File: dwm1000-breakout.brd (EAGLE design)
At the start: 26.2 x 21.6 mm, 9 parts, among them U2 DWM1000

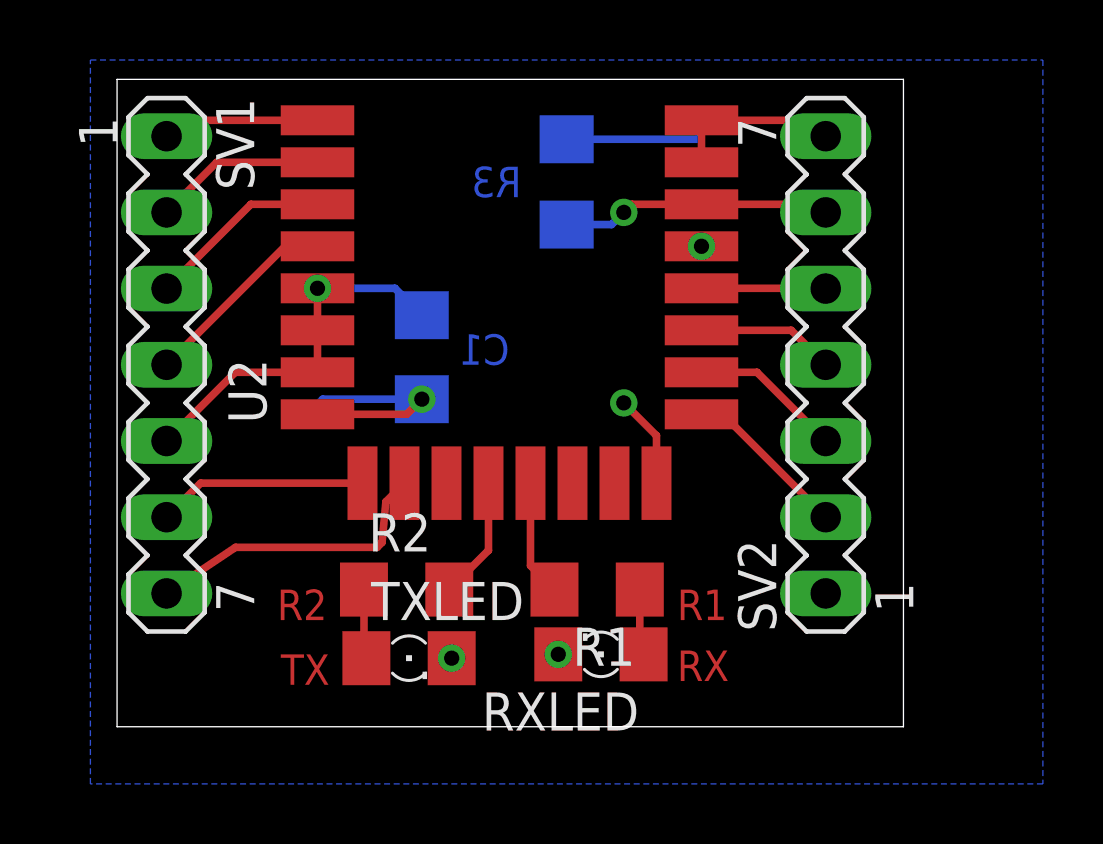
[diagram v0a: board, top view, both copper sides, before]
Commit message: renamed and laid out a little better i hope
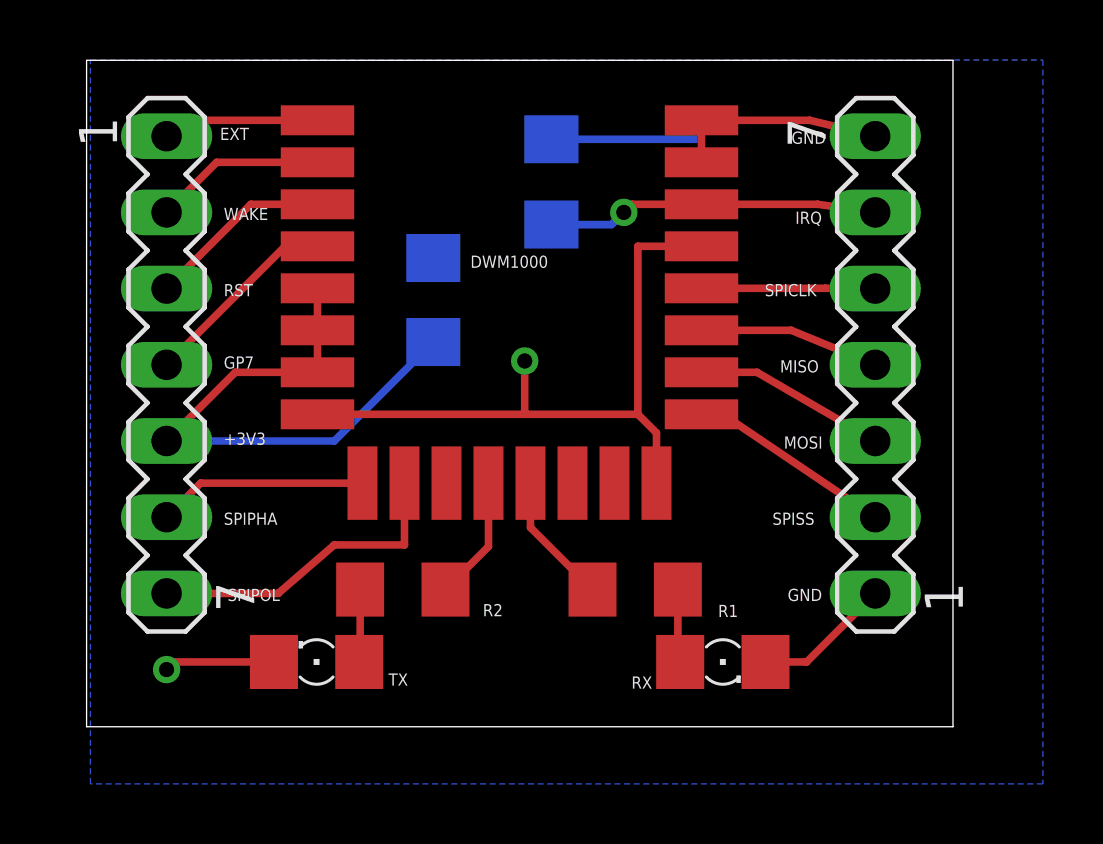
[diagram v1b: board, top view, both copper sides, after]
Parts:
- removed RXLED, TXLED: (no value), led:1206
- added RX, TX: (no value), led:1206
- moved C1 1.94 mm to (10.2, 17.4), turned to 90 degrees
- moved SV2 1.65 mm to (24.9, 15.2)
- moved R1 1.27 mm to (16.9, 7.75)
- moved R3 0.51 mm to (14.1, 21.3)
- moved R2 0.13 mm to (9.14, 7.75)
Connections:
- net GND: now also RX.C, TX.C; no longer RXLED.C, TXLED.C
- net N$1: now also RX.A; no longer RXLED.A
- net N$2: now also TX.A; no longer TXLED.A
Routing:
- net GND: track 20.5 -> 43.3 mm, vias 5 -> 2
- net +3V3: track 12.6 -> 19.0 mm, vias 1 -> 0
- net IRQ: track 9.03 -> 11.1 mm
- net SPICLK: track 4.15 -> 5.79 mm
- net MISO: track 4.62 -> 6.02 mm
- net MOSI: track 5.09 -> 6.41 mm
- net SPISS: track 5.56 -> 6.84 mm
- net SPIPOL: track 9.95 -> 10.6 mm
- net RXLED: track 3.88 -> 4.41 mm
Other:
- board size 26.2 x 21.6 mm -> 28.9 x 22.2 mm
- board text added: "+3V3"
- board text added: "EXT"
- board text added: "GND"
- board text added: "GP7"
- board text added: "IRQ"
- board text added: "MISO"
- board text added: "MOSI"
- board text added: "RST"
- board text added: "SPICLK"
- board text added: "SPIPHA"
- board text added: "SPIPOL"
- board text added: "SPISS"
- board text added: "WAKE"
- board text removed: "C1"
- board text removed: "R1"
- board text removed: "R2"
- board text removed: "R3"
- board text removed: "RX"
- board text removed: "TX"

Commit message: used oshpark's DRU file
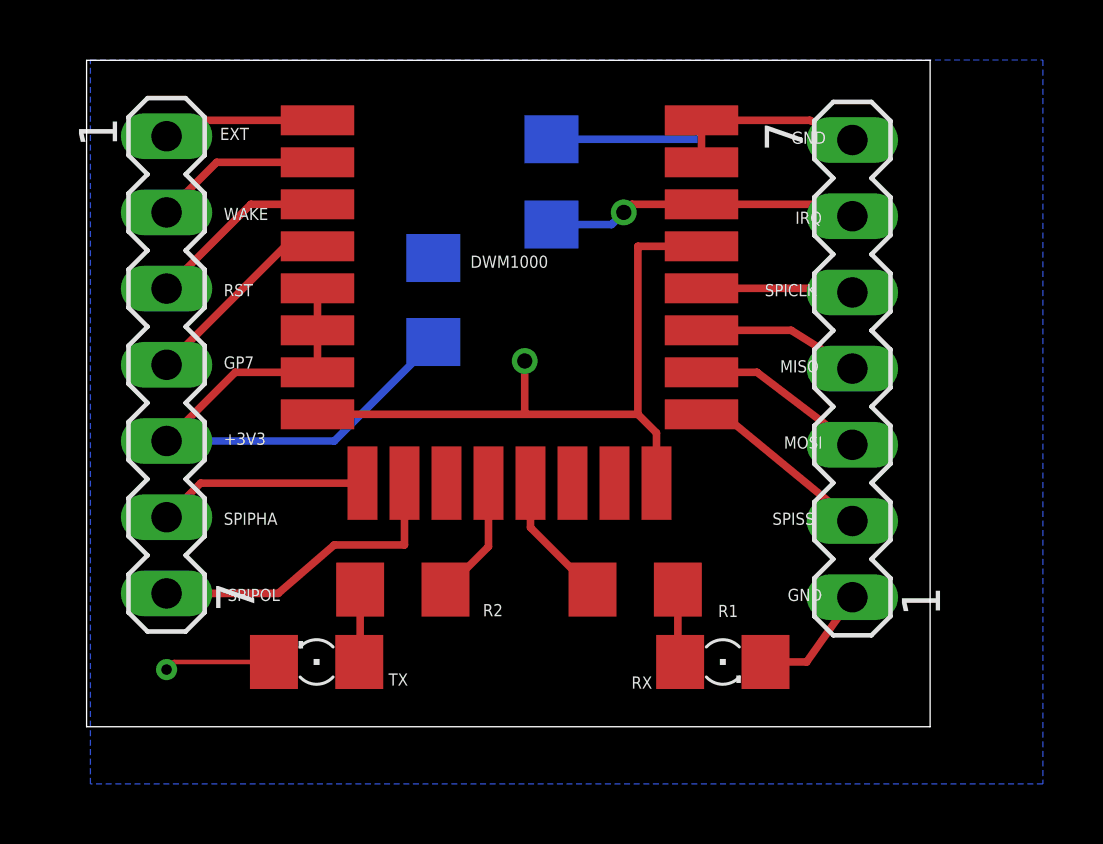
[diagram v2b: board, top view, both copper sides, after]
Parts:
- C1: value (none) -> 0.1uF
- R1, R2: value (none) -> 470
- R3: value (none) -> 100k
- moved SV2 0.77 mm to (24.1, 15.1)
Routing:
- net GND: track 43.3 -> 42.0 mm
- net SPICLK: track 5.79 -> 5.04 mm
- net IRQ: track 11.1 -> 10.4 mm
- net MISO: track 6.02 -> 5.40 mm
- net MOSI: track 6.41 -> 5.84 mm
- net SPISS: track 6.84 -> 6.31 mm
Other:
- board size 28.9 x 22.2 mm -> 28.1 x 22.2 mm

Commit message: added a power indicator LED
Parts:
- added PWR: (no value), led:1206
- added R4: (no value), rcl:R1206
- moved TX 13.7 mm to (19.8, 7.11), turned to 90 degrees
- moved R2 3.24 mm to (12.3, 7.11), turned to 90 degrees
- moved RX 2.80 mm to (17.7, 7.11), turned to 90 degrees
- moved R1 2.01 mm to (15.0, 7.11), turned to 90 degrees
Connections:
- new net N$3: PWR.A, R4.2
- net +3V3: now also R4.1
- net GND: now also PWR.C
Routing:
- net N$3: track 0.00 -> 7.75 mm, vias 0 -> 1
- net N$2: track 2.43 -> 8.39 mm
- net +3V3: track 19.0 -> 24.5 mm, vias 0 -> 1
- net GND: track 42.0 -> 47.0 mm
- net TXLED: track 4.14 -> 2.89 mm
- net RXLED: track 4.41 -> 3.42 mm
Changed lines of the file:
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@@
 <layer number="25" name="tNames" color="7" fill="1" visible="yes" active="yes"/>
 <layer number="26" name="bNames" color="7" fill="1" visible="yes" active="yes"/>
-<layer number="27" name="tValues" color="7" fill="1" visible="yes" active="yes"/>
-<layer number="28" name="bValues" color="7" fill="1" visible="yes" active="yes"/>
+<layer number="27" name="tValues" color="7" fill="1" visible="no" active="yes"/>
+<layer number="28" name="bValues" color="7" fill="1" visible="no" active="yes"/>
 <layer number="29" name="tStop" color="7" fill="3" visible="no" active="yes"/>
 <layer number="30" name="bStop" color="7" fill="6" visible="no" active="yes"/>
@@
 <attribute name="VALUE" x="7.62" y="16.129" size="1.27" layer="28" rot="MR90"/>
 </element>
-<element name="RX" library="led" library_urn="urn:adsk.eagle:library:259" package="1206" value="" x="19.812" y="5.334" smashed="yes">
-<attribute name="NAME" x="16.764" y="4.445" size="0.4064" layer="25" font="vector"/>
-<attribute name="VALUE" x="18.542" y="2.794" size="1.27" layer="27"/>
-</element>
-<element name="TX" library="led" library_urn="urn:adsk.eagle:library:259" package="1206" value="" x="6.27" y="5.334" smashed="yes" rot="R180">
-<attribute name="NAME" x="9.318" y="4.953" size="0.4064" layer="25" rot="R180"/>
-<attribute name="VALUE" x="7.54" y="7.874" size="1.27" layer="27" rot="R180"/>
-</element>
-<element name="R1" library="rcl" library_urn="urn:adsk.eagle:library:334" package="R1206" value="470" x="16.891" y="7.747" smashed="yes" rot="R180">
-<attribute name="NAME" x="20.32" y="7.239" size="0.4064" layer="25" rot="R180"/>
-<attribute name="VALUE" x="18.161" y="10.287" size="1.27" layer="27" rot="R180"/>
-</element>
-<element name="R2" library="rcl" library_urn="urn:adsk.eagle:library:334" package="R1206" value="470" x="9.144" y="7.747" smashed="yes">
-<attribute name="NAME" x="11.811" y="6.858" size="0.4064" layer="25"/>
-<attribute name="VALUE" x="7.874" y="5.207" size="1.27" layer="27"/>
+<element name="RX" library="led" library_urn="urn:adsk.eagle:library:259" package="1206" value="" x="17.653" y="7.112" smashed="yes" rot="R90">
+<attribute name="NAME" x="18.415" y="4.699" size="0.4064" layer="25" font="vector" rot="R180"/>
+<attribute name="VALUE" x="20.193" y="5.842" size="1.27" layer="27" rot="R90"/>
+</element>
+<element name="TX" library="led" library_urn="urn:adsk.eagle:library:259" package="1206" value="" x="19.812" y="7.112" smashed="yes" rot="R90">
+<attribute name="NAME" x="20.574" y="4.699" size="0.4064" layer="25" rot="R180"/>
+<attribute name="VALUE" x="22.352" y="5.842" size="1.27" layer="27" rot="R90"/>
+</element>
+<element name="R1" library="rcl" library_urn="urn:adsk.eagle:library:334" package="R1206" value="470" x="14.986" y="7.112" smashed="yes" rot="R90">
+<attribute name="NAME" x="14.859" y="4.445" size="0.4064" layer="25" rot="R180"/>
+<attribute name="VALUE" x="17.526" y="5.842" size="1.27" layer="27" rot="R90"/>
+</element>
+<element name="R2" library="rcl" library_urn="urn:adsk.eagle:library:334" package="R1206" value="470" x="12.319" y="7.112" smashed="yes" rot="R90">
+<attribute name="NAME" x="11.43" y="4.064" size="0.4064" layer="25"/>
+<attribute name="VALUE" x="14.859" y="5.842" size="1.27" layer="27" rot="R90"/>
 </element>
 <element name="R3" library="rcl" library_urn="urn:adsk.eagle:library:334" package="R1206" value="100k" x="14.097" y="21.336" smashed="yes" rot="MR270">
@@
 <attribute name="PRICE" value="20.95 USD" x="12.7" y="21.59" size="1.778" layer="27" display="off"/>
 <attribute name="VALUE" x="13.988" y="18.879" size="0.4064" layer="25" rot="R180"/>
+</element>
+<element name="PWR" library="led" library_urn="urn:adsk.eagle:library:259" package="1206" value="" x="5.588" y="4.826" smashed="yes" rot="R180">
+<attribute name="NAME" x="7.874" y="3.81" size="0.4064" layer="25" font="vector" rot="R180"/>
+<attribute name="VALUE" x="6.858" y="7.366" size="1.27" layer="27" rot="R180"/>
+</element>
+<element name="R4" library="rcl" library_urn="urn:adsk.eagle:library:334" package="R1206" value="" x="5.588" y="7.239" smashed="yes" rot="MR180">
+<attribute name="NAME" x="5.969" y="5.588" size="0.4064" layer="26" font="vector" rot="MR0"/>
+<attribute name="VALUE" x="4.318" y="9.779" size="1.27" layer="28" rot="MR180"/>
 </element>
 </elements>
@@
 <wire x1="22.711" y1="23.39" x2="24.13" y2="22.733" width="0.254" layer="1"/>
 <wire x1="19.1" y1="21.99" x2="19.1" y2="23.39" width="0.254" layer="1"/>
-<wire x1="21.234" y1="5.334" x2="22.606" y2="5.334" width="0.254" layer="1"/>
-<wire x1="22.606" y1="5.334" x2="24.13" y2="7.493" width="0.254" layer="1"/>
 <wire x1="17.6" y1="12.96986875" x2="17.6" y2="11.295" width="0.254" layer="1"/>
 <wire x1="6.3" y1="13.59" x2="13.208" y2="13.59" width="0.254" layer="1"/>
@@
 <wire x1="19.1" y1="19.19" x2="16.97986875" y2="19.19" width="0.254" layer="1"/>
 <wire x1="16.97986875" y1="19.19" x2="16.97986875" y2="13.59" width="0.254" layer="1"/>
-<wire x1="4.848" y1="5.334" x2="1.524" y2="5.334" width="0.1524" layer="1"/>
-<wire x1="1.524" y1="5.334" x2="1.27" y2="5.08" width="0.1524" layer="1"/>
+<contactref element="PWR" pad="C"/>
+<wire x1="4.166" y1="4.826" x2="1.524" y2="4.826" width="0.254" layer="1"/>
+<wire x1="1.524" y1="4.826" x2="1.27" y2="5.08" width="0.254" layer="1"/>
 <via x="1.27" y="5.08" extent="1-16" drill="0.35"/>
+<wire x1="17.653" y1="8.534" x2="19.812" y2="8.534" width="0.254" layer="1"/>
+<wire x1="19.812" y1="8.534" x2="23.089" y2="8.534" width="0.254" layer="1"/>
+<wire x1="23.089" y1="8.534" x2="24.13" y2="7.493" width="0.254" layer="1"/>
+<wire x1="17.6" y1="11.295" x2="17.6" y2="8.587" width="0.254" layer="1"/>
+<wire x1="17.6" y1="8.587" x2="17.653" y2="8.534" width="0.254" layer="1"/>
 </signal>
 <signal name="+3V3">
@@
 <wire x1="6.3" y1="16.39" x2="6.3" y2="14.99" width="0.254" layer="1"/>
 <wire x1="6.3" y1="16.39" x2="6.3" y2="17.79" width="0.254" layer="1"/>
-<wire x1="1.27" y1="12.7" x2="6.861" y2="12.7" width="0.254" layer="16"/>
+<wire x1="4.15514375" y1="12.7" x2="1.27" y2="12.7" width="0.254" layer="16"/>
+<wire x1="4.15514375" y1="12.7" x2="6.861" y2="12.7" width="0.254" layer="16"/>
 <wire x1="6.861" y1="12.7" x2="10.16" y2="15.999" width="0.254" layer="16"/>
+<contactref element="R4" pad="1"/>
+<wire x1="4.166" y1="7.239" x2="4.166" y2="12.68914375" width="0.254" layer="16"/>
+<wire x1="4.166" y1="12.68914375" x2="4.15514375" y2="12.7" width="0.254" layer="16"/>
+<via x="4.166" y="12.68914375" extent="1-16" drill="0.35"/>
 </signal>
 <signal name="MOSI">
@@
 <contactref element="U2" pad="12"/>
 <contactref element="R2" pad="2"/>
-<wire x1="12" y1="11.295" x2="12" y2="9.181" width="0.254" layer="1"/>
-<wire x1="12" y1="9.181" x2="10.566" y2="7.747" width="0.254" layer="1"/>
+<wire x1="12" y1="11.295" x2="12" y2="8.853" width="0.254" layer="1"/>
+<wire x1="12" y1="8.853" x2="12.319" y2="8.534" width="0.254" layer="1"/>
 </signal>
 <signal name="RXLED">
 <contactref element="U2" pad="13"/>
 <contactref element="R1" pad="2"/>
-<wire x1="13.4" y1="11.295" x2="13.4" y2="9.816" width="0.254" layer="1"/>
-<wire x1="13.4" y1="9.816" x2="15.469" y2="7.747" width="0.254" layer="1"/>
+<wire x1="13.4" y1="11.295" x2="13.4" y2="10.12" width="0.254" layer="1"/>
+<wire x1="13.4" y1="10.12" x2="14.986" y2="8.534" width="0.254" layer="1"/>
 </signal>
 <signal name="EXT">
@@
 <contactref element="R1" pad="1"/>
 <contactref element="RX" pad="A"/>
-<wire x1="18.313" y1="7.747" x2="18.313" y2="5.411" width="0.254" layer="1"/>
-<wire x1="18.313" y1="5.411" x2="18.39" y2="5.334" width="0.254" layer="1"/>
+<wire x1="14.986" y1="5.69" x2="17.653" y2="5.69" width="0.254" layer="1"/>
 </signal>
 <signal name="N$2">
 <contactref element="R2" pad="1"/>
 <contactref element="TX" pad="A"/>
-<wire x1="7.722" y1="7.747" x2="7.722" y2="5.364" width="0.254" layer="1"/>
-<wire x1="7.722" y1="5.364" x2="7.692" y2="5.334" width="0.254" layer="1"/>
+<wire x1="12.319" y1="5.69" x2="12.88936875" y2="5.69" width="0.254" layer="1"/>
+<wire x1="19.74963125" y1="5.69" x2="19.812" y2="5.69" width="0.254" layer="1"/>
+<wire x1="12.88936875" y1="5.69" x2="13.96876875" y2="4.6106" width="0.254" layer="1"/>
+<wire x1="18.67023125" y1="4.6106" x2="19.74963125" y2="5.69" width="0.254" layer="1"/>
+<wire x1="13.96876875" y1="4.6106" x2="18.67023125" y2="4.6106" width="0.254" layer="1"/>
+</signal>
+<signal name="N$3">
+<contactref element="R4" pad="2"/>
+<contactref element="PWR" pad="A"/>
+<wire x1="7.01" y1="4.826" x2="9.677" y2="4.826" width="0.254" layer="1"/>
+<via x="9.677" y="4.826" extent="1-16" drill="0.35"/>
+<wire x1="7.01" y1="7.239" x2="9.677" y2="7.239" width="0.254" layer="16"/>
+<wire x1="9.677" y1="7.239" x2="9.677" y2="4.826" width="0.254" layer="16"/>
 </signal>
 </signals>

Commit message: Rand's nitpicking
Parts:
- removed C1: 0.1uF, rcl:C1206
- added C2: (no value), Passives:C1210
- moved TX 7.15 mm to (12.7, 6.35), turned to 270 degrees
- moved PWR 3.18 mm to (8.38, 6.35), turned to 270 degrees
- moved R4 2.93 mm to (8.38, 6.35), turned to 90 degrees
- moved R3 2.56 mm to (15.2, 19.1)
- moved R1 2.17 mm to (17.0, 6.35), flipped to the bottom, turned to 270 degrees
- moved RX 0.99 mm to (17.0, 6.35), turned to 270 degrees
- moved R2 0.85 mm to (12.7, 6.35), flipped to the bottom, turned to 270 degrees
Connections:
- net +3V3: now also C2.P$1; no longer C1.1
- net GND: now also C2.P$2; no longer C1.2, RX.C, TX.C
- net N$1: now also R1.2, RX.C; no longer R1.1, RX.A
- net N$2: now also R2.2, TX.C; no longer R2.1, TX.A
- net RXLED: now also RX.A; no longer R1.2
- net TXLED: now also TX.A; no longer R2.2
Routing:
- net GND: track 47.0 -> 0.00 mm, vias 2 -> 5
- net IRQ: track 10.4 -> 15.9 mm
- net N$2: track 8.39 -> 4.19 mm, vias 0 -> 1
- net +3V3: track 24.5 -> 28.3 mm
- net N$1: track 2.67 -> 5.38 mm, vias 0 -> 1
- net N$3: track 7.75 -> 5.21 mm
- net RXLED: track 3.42 -> 5.93 mm
- net TXLED: track 2.89 -> 3.81 mm
- net GP7: track 6.67 -> 7.56 mm
- added copper zone on layer 1, net GND

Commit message: Whoops left some things unconnected. Fixed.
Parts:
- C2: value (none) -> 0.1uF
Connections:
- net GND: now also R1.1, R2.1
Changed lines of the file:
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@@
 <attribute name="VALUE" x="5.842" y="5.08" size="1.27" layer="28" rot="MR90"/>
 </element>
-<element name="C2" library="Passives" package="C1210" value="" x="10.16" y="19.05" rot="MR90">
+<element name="C2" library="Passives" package="C1210" value="0.1uF" x="10.16" y="19.05" rot="MR90">
 <attribute name="DIGIKEY" value="N/A" x="10.16" y="19.05" size="1.778" layer="28" rot="MR90" display="off"/>
 <attribute name="MPN" value="N/A" x="10.16" y="19.05" size="1.778" layer="28" rot="MR90" display="off"/>
@@
 <via x="15.24" y="22.86" extent="1-16" drill="0.635"/>
 <via x="12.7" y="15.24" extent="1-16" drill="0.635"/>
+<contactref element="R2" pad="1"/>
+<contactref element="R1" pad="1"/>
 </signal>
 <signal name="+3V3">

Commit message: Added part info
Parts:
- removed SV1, SV2: (no value), con-lstb:MA07-1
- added J1, J2: (no value), SparkFun-Connectors:1X07_LOCK
- PWR, RX, TX: value (none) -> GREEN; device led:1206 -> SparkFun-LED:LED-1206
- R1, R2: value 470 -> 65; device rcl:R1206 -> SparkFun-Resistors:1206
- R3: device rcl:R1206 -> SparkFun-Resistors:1206
- R4: value (none) -> 65; device rcl:R1206 -> SparkFun-Resistors:1206
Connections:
- net +3V3: now also J2.3; no longer SV1.5
- net EXT: now also J2.7; no longer SV1.1
- net GND: now also J1.1, J1.7; no longer SV2.1, SV2.7
- net GP7: now also J2.4; no longer SV1.4
- net IRQ: now also J1.6; no longer SV2.6
- net MISO: now also J1.4; no longer SV2.4
- net MOSI: now also J1.3; no longer SV2.3
- net RST: now also J2.5; no longer SV1.3
- net SPICLK: now also J1.5; no longer SV2.5
- net SPIPHA: now also J2.2; no longer SV1.6
- net SPIPOL: now also J2.1; no longer SV1.7
- net SPISS: now also J1.2; no longer SV2.2
- net WAKE: now also J2.6; no longer SV1.2
